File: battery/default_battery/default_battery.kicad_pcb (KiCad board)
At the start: 2 copper layers, 14 parts

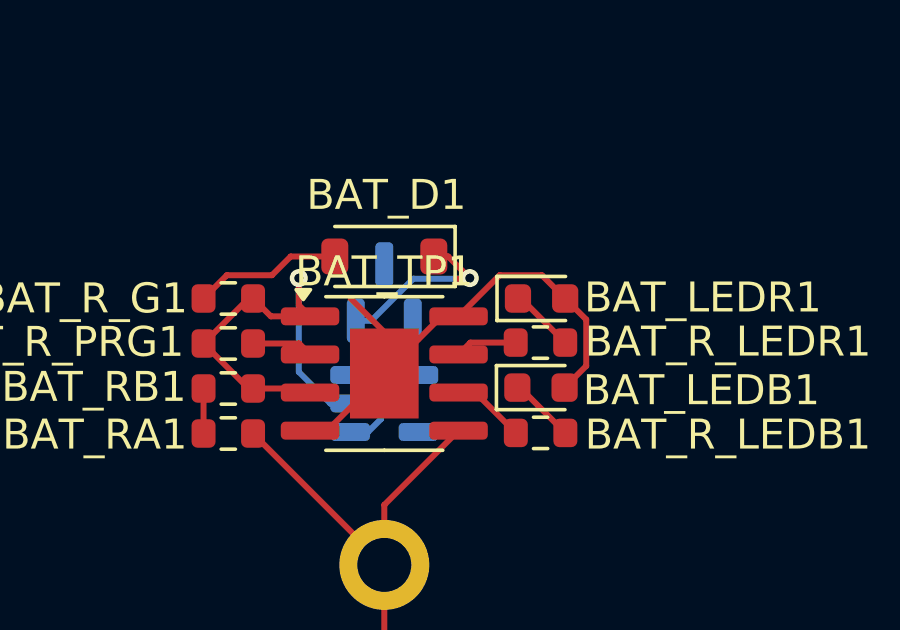
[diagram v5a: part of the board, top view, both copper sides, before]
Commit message: adjust battery via pos
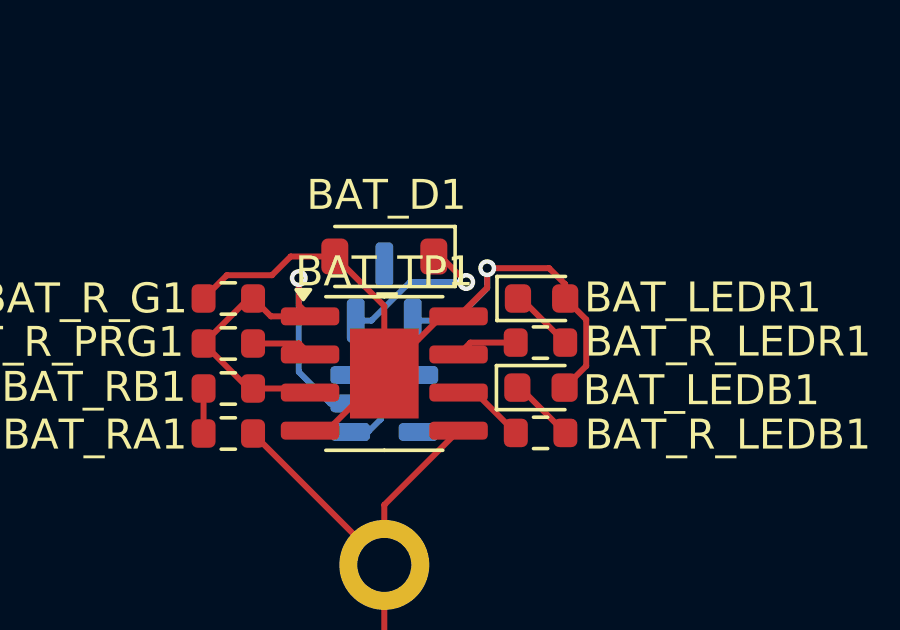
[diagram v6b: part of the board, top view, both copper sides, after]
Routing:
- net VBUS: track 22.5 -> 28.5 mm, vias 0 -> 1
- net Net-(BAT_AP1-EN): track 11.7 -> 11.0 mm
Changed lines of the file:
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@@
-	)
-	(segment
-		(start -1.126 -40.506)
-		(end 0 -39.38)
-		(width 0.2)
-		(layer "F.Cu")
-		(net 4)
 	)
 	(segment
@@
 	)
 	(segment
+		(start 5.494999 -41.51)
+		(end 3.43 -41.51)
+		(width 0.2)
+		(layer "F.Cu")
+		(net 4)
+	)
+	(segment
 		(start 6.731 -39.799)
 		(end 6.03 -40.5)
@@
 	)
 	(segment
-		(start 5.254 -41.276)
-		(end 3.846 -41.276)
-		(width 0.2)
-		(layer "F.Cu")
-		(net 4)
-	)
-	(segment
 		(start 6.03 -40.5)
-		(end 5.254 -41.276)
+		(end 6.03 -40.974999)
+		(width 0.2)
+		(layer "F.Cu")
+		(net 4)
+	)
+	(segment
+		(start 2.475 -39.905)
+		(end 3.43 -40.86)
 		(width 0.2)
 		(layer "F.Cu")
@@
 	)
 	(segment
+		(start 0 -40.25)
+		(end -1.65 -41.9)
+		(width 0.2)
+		(layer "F.Cu")
+		(net 4)
+	)
+	(segment
 		(start -6.025 -40.5)
 		(end -5.249 -41.276)
@@
 	)
 	(segment
-		(start 0 -39.38)
-		(end 0 -38)
-		(width 0.2)
-		(layer "F.Cu")
-		(net 4)
-	)
-	(segment
 		(start -3.744 -41.276)
 		(end -3.12 -41.9)
@@
 	)
 	(segment
+		(start 3.43 -40.86)
+		(end 3.43 -41.51)
+		(width 0.2)
+		(layer "F.Cu")
+		(net 4)
+	)
+	(segment
 		(start 6.01 -37.53)
 		(end 6.731 -38.251)
@@
 	)
 	(segment
-		(start 3.846 -41.276)
-		(end 2.475 -39.905)
-		(width 0.2)
-		(layer "F.Cu")
-		(net 4)
-	)
-	(segment
-		(start 1.65 -41.9)
-		(end 2.13 -41.9)
-		(width 0.2)
-		(layer "F.Cu")
-		(net 7)
-	)
-	(segment
-		(start 2.13 -41.9)
-		(end 2.85 -41.18)
-		(width 0.2)
-		(layer "F.Cu")
-		(net 7)
-	)
-	(segment
-		(start 2.39 -41.16)
-		(end 2.83 -41.16)
-		(width 0.2)
-		(layer "F.Cu")
-		(net 7)
+		(start 6.03 -40.974999)
+		(end 5.494999 -41.51)
+		(width 0.2)
+		(layer "F.Cu")
+		(net 4)
+	)
+	(segment
+		(start 0 -38)
+		(end 0 -40.25)
+		(width 0.2)
+		(layer "F.Cu")
+		(net 4)
 	)
 	(via
-		(at 2.85 -41.18)
+		(at 3.43 -41.51)
 		(size 0.6)
 		(drill 0.3)
 		(layers "F.Cu" "B.Cu")
+		(net 4)
+	)
+	(segment
+		(start 3.43 -40.840761)
+		(end 3.43 -41.51)
+		(width 0.2)
+		(layer "B.Cu")
+		(net 4)
+	)
+	(segment
+		(start 2.351739 -39.7625)
+		(end 3.43 -40.840761)
+		(width 0.2)
+		(layer "B.Cu")
+		(net 4)
+	)
+	(segment
+		(start 0.95 -39.7625)
+		(end 2.351739 -39.7625)
+		(width 0.2)
+		(layer "B.Cu")
+		(net 4)
+	)
+	(segment
+		(start 1.65 -41.9)
+		(end 1.88 -41.9)
+		(width 0.2)
+		(layer "F.Cu")
+		(net 7)
+	)
+	(segment
+		(start 1.88 -41.9)
+		(end 2.73 -41.05)
+		(width 0.2)
+		(layer "F.Cu")
+		(net 7)
+	)
+	(via
+		(at 2.73 -41.05)
+		(size 0.6)
+		(drill 0.3)
+		(layers "F.Cu" "B.Cu")
 		(net 7)
 	)
@@
 	)
 	(segment
+		(start -0.95 -39.7625)
+		(end -0.429468 -39.7625)
+		(width 0.2)
+		(layer "B.Cu")
+		(net 7)
+	)
+	(segment
+		(start -1.1375 -36.05)
+		(end -0.54 -36.05)
+		(width 0.2)
+		(layer "B.Cu")
+		(net 7)
+	)
+	(segment
 		(start -0.95 -38.1375)
 		(end -1.1375 -37.95)
@@
 	)
 	(segment
+		(start -0.11 -36.48)
+		(end -0.11 -37.584999)
+		(width 0.2)
+		(layer "B.Cu")
+		(net 7)
+	)
+	(segment
+		(start -0.429468 -39.7625)
+		(end 0.858032 -41.05)
+		(width 0.2)
+		(layer "B.Cu")
+		(net 7)
+	)
+	(segment
+		(start 0.858032 -41.05)
+		(end 2.73 -41.05)
+		(width 0.2)
+		(layer "B.Cu")
+		(net 7)
+	)
+	(segment
 		(start -0.475001 -37.95)
 		(end -1.1375 -37.95)
@@
 		(width 0.2)
 		(layer "B.Cu")
-		(net 7)
-	)
-	(segment
-		(start -0.95 -39.7625)
-		(end -0.429468 -39.7625)
-		(width 0.2)
-		(layer "B.Cu")
-		(net 7)
-	)
-	(segment
-		(start 0.968032 -41.16)
-		(end 2.83 -41.16)
-		(width 0.2)
-		(layer "B.Cu")
-		(net 7)
-	)
-	(segment
-		(start -0.11 -36.48)
-		(end -0.11 -37.584999)
-		(width 0.2)
-		(layer "B.Cu")
-		(net 7)
-	)
-	(segment
-		(start -0.429468 -39.7625)
-		(end 0.968032 -41.16)
-		(width 0.2)
-		(layer "B.Cu")
-		(net 7)
-	)
-	(segment
-		(start -1.1375 -36.05)
-		(end -0.54 -36.05)
-		(width 0.2)
-		(layer "B.Cu")

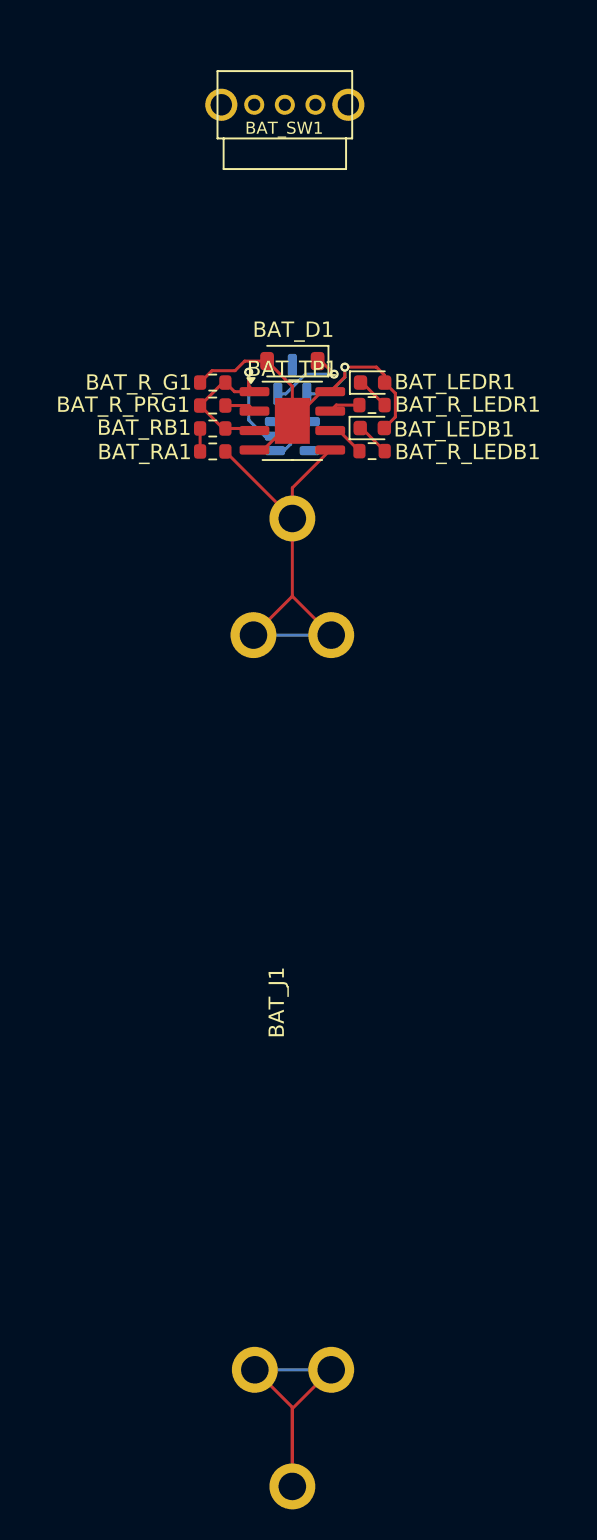
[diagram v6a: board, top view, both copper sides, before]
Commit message: adjust battery via pos
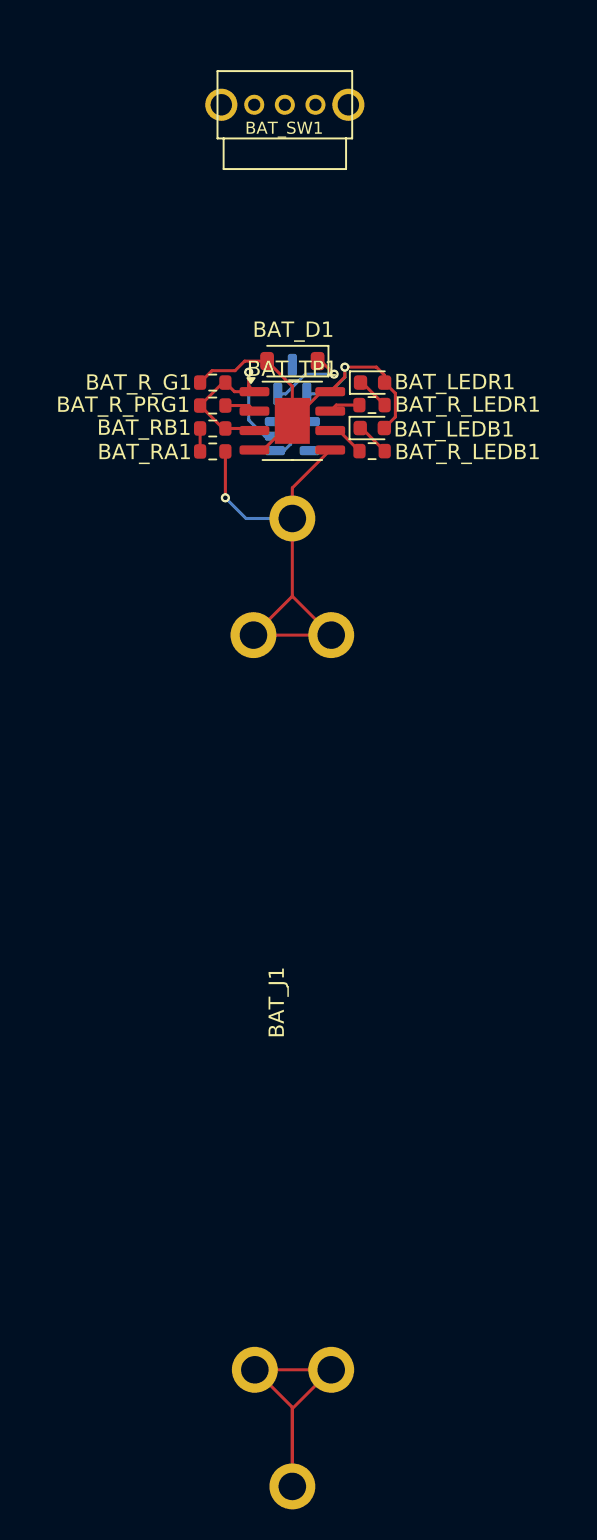
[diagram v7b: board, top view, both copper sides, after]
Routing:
- net VBAT: track 29.0 -> 30.8 mm, vias 0 -> 1
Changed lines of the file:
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@@
-	)
-	(segment
-		(start -4.375 -35.995)
-		(end 0 -31.62)
-		(width 0.2)
-		(layer "F.Cu")
-		(net 1)
 	)
 	(segment
@@
 	(segment
 		(start -4.375 -36)
-		(end -4.375 -35.995)
+		(end -4.375 -32.97)
 		(width 0.2)
 		(layer "F.Cu")
@@
 	)
 	(segment
+		(start -2.54 -24)
+		(end 2.54 -24)
+		(width 0.2)
+		(layer "F.Cu")
+		(net 1)
+	)
+	(segment
 		(start 0 -26.54)
 		(end 0 -31.62)
@@
 		(net 1)
 	)
+	(via
+		(at -4.375 -32.97)
+		(size 0.6)
+		(drill 0.3)
+		(layers "F.Cu" "B.Cu")
+		(net 1)
+	)
 	(segment
-		(start -2.54 -24)
-		(end 2.54 -24)
+		(start 0 -31.62)
+		(end -3.025 -31.62)
+		(width 0.2)
+		(layer "B.Cu")
+		(net 1)
+	)
+	(segment
+		(start -3.025 -31.62)
+		(end -4.375 -32.97)
 		(width 0.2)
 		(layer "B.Cu")
@@
 		(start -4.375 -40.5)
 		(end -4.525 -40.5)
+		(width 0.2)
+		(layer "F.Cu")
+		(net 2)
+	)
+	(segment
+		(start -2.45 24)
+		(end 2.54 24)
 		(width 0.2)
 		(layer "F.Cu")
@@
 		(width 0.2)
 		(layer "B.Cu")
-		(net 2)
-	)
-	(segment
-		(start -2.45 24)
-		(end 2.54 24)
-		(width 0.2)
-		(layer "B.Cu")

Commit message: replace VDD-nRF to VCC
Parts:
- BAT_SW1: value SW_DPDT_x2 -> ~
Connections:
- net BT_PIN renamed ADC_BT
- net nRF_VDD renamed VCC
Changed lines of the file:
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@@
 	(net 1 "VBAT")
 	(net 2 "GND")
-	(net 3 "BT_PIN")
+	(net 3 "VCC")
 	(net 4 "VBUS")
 	(net 5 "Net-(BAT_Q1-D)")
-	(net 6 "nRF_VDD")
+	(net 6 "ADC_BT")
 	(net 7 "Net-(BAT_AP1-EN)")
 	(net 8 "unconnected-(BAT_AP1-NC-Pad4)")
@@
 			(layers "F.Cu" "F.Mask" "F.Paste")
 			(roundrect_rratio 0.25)
-			(net 3 "BT_PIN")
+			(net 6 "ADC_BT")
 			(pintype "passive")
 		)
@@
 			)
 		)
-		(property "Value" "SW_DPDT_x2"
+		(property "Value" "~"
 			(at 0.01 3.18 0)
 			(layer "F.Fab")
@@
 			(layers "F.Cu" "F.Mask" "F.Paste")
 			(roundrect_rratio 0.25)
-			(net 3 "BT_PIN")
+			(net 6 "ADC_BT")
 			(pintype "passive")
 		)
@@
 			(layers "B.Cu" "B.Mask" "B.Paste")
 			(roundrect_rratio 0.25)
-			(net 6 "nRF_VDD")
+			(net 3 "VCC")
 			(pinfunction "VOUT")
 			(pintype "power_out")
@@
 	)
 	(segment
-		(start -6.025 -37.5)
-		(end -6.025 -36)
-		(width 0.2)
-		(layer "F.Cu")
-		(net 3)
-	)
-	(segment
 		(start -2.475 -36.095)
 		(end -1.905 -36.095)
@@
 	)
 	(segment
+		(start -6.025 -37.5)
+		(end -6.025 -36)
+		(width 0.2)
+		(layer "F.Cu")
+		(net 6)
+	)
+	(segment
